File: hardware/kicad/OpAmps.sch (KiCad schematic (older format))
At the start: 63 parts, among them P1 Out X, P2 Out Y, P3 Out Red, P4 Out Green, P5 Out Blue, P6 Out C1, U2 LT1356CN, U3 LT1356CN, U4 LT1356CN

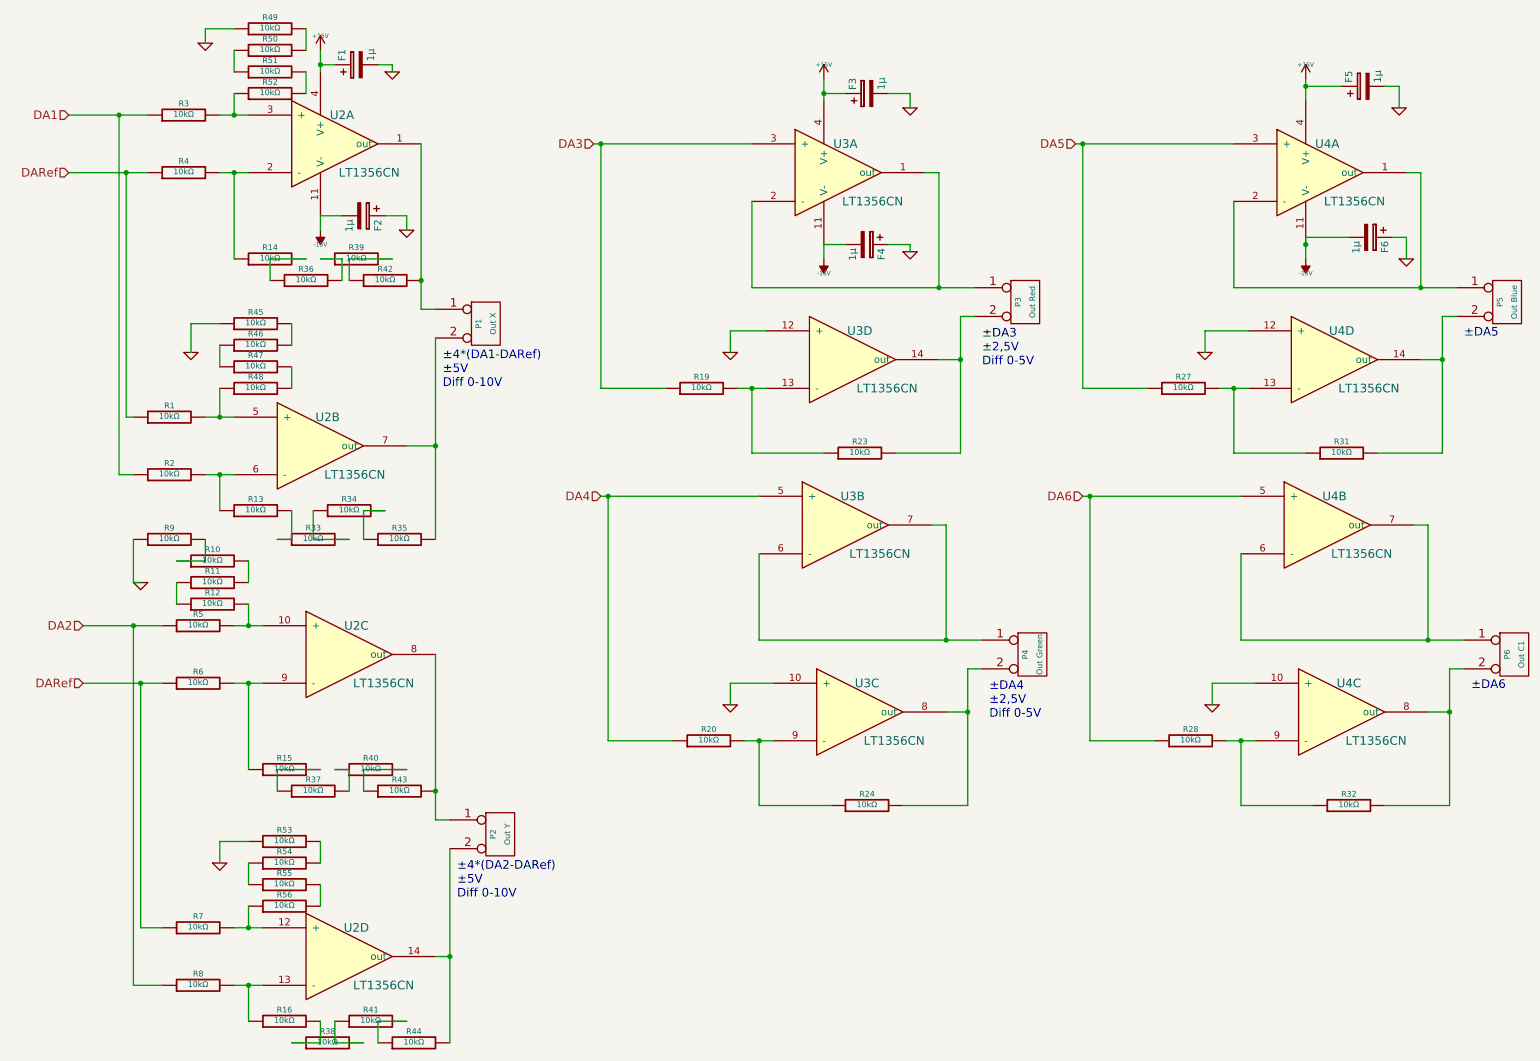
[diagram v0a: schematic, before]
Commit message: add output protection
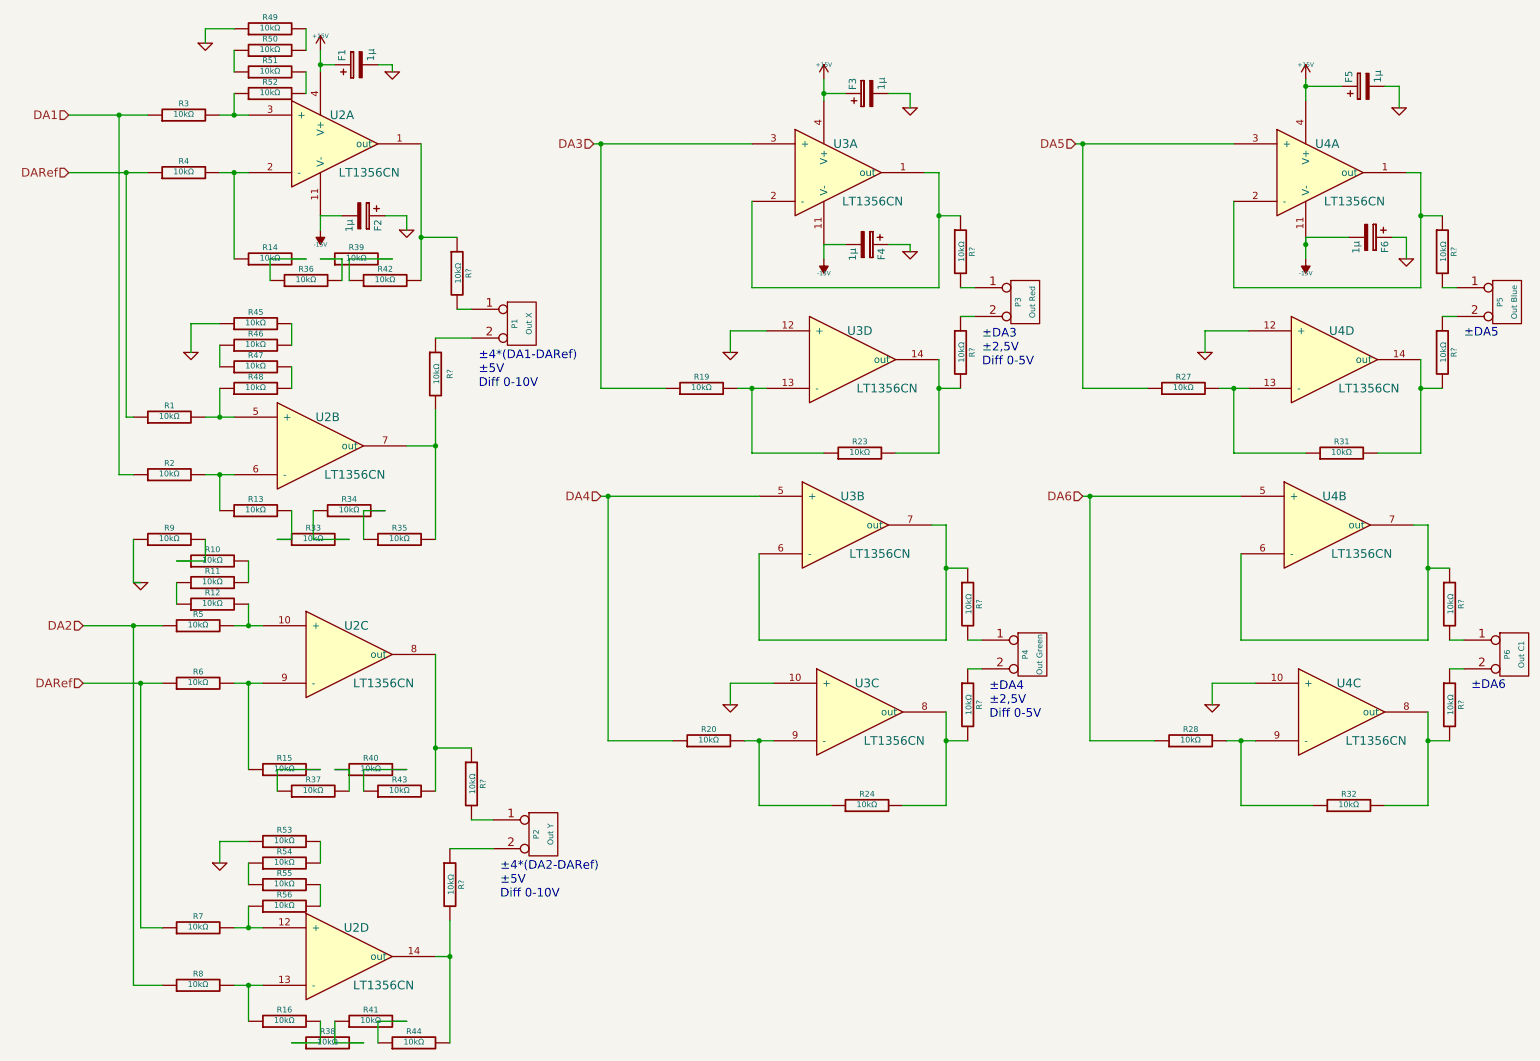
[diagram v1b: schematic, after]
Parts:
- added R? (x4): 10kΩ, Resistors_SMD:R_0603_HandSoldering, symbol R-RESCUE-ildagenerator
- added R? (x8): 10kΩ, symbol R-RESCUE-ildagenerator
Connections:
- net at R43.2, U2.8 (out): now also R?.1; no longer P2.1 (P1)
- net at R35.2, U2.7 (out): now also R?.2; no longer P1.2 (PM)
- net at R44.2, U2.14 (out): now also R?.2; no longer P2.2 (PM)
- net at R42.2, U2.1 (out): now also R?.1; no longer P1.1 (P1)
- net at U3.1 (out), U3.2 (-): now also R?.1; no longer P3.1 (P1)
- net at R24.2, U3.8 (out): now also R?.2; no longer P4.2 (PM)
- net at R23.2, U3.14 (out): now also R?.2; no longer P3.2 (PM)
- net at U3.6 (-), U3.7 (out): now also R?.1; no longer P4.1 (P1)
- net at U4.1 (out), U4.2 (-): now also R?.1; no longer P5.1 (P1)
- net at R32.2, U4.8 (out): now also R?.2; no longer P6.2 (PM)
- net at R31.2, U4.14 (out): now also R?.2; no longer P5.2 (PM)
- net at U4.6 (-), U4.7 (out): now also R?.1; no longer P6.1 (P1)
- new net: P1.1 (P1), R?.2
- new net: P1.2 (PM), R?.1
- new net: P2.1 (P1), R?.2
- new net: P2.2 (PM), R?.1
- new net: P3.1 (P1), R?.2
- new net: P3.2 (PM), R?.1
- new net: P4.1 (P1), R?.2
- new net: P4.2 (PM), R?.1
- new net: P5.1 (P1), R?.2
- new net: P5.2 (PM), R?.1
- new net: P6.1 (P1), R?.2
- new net: P6.2 (PM), R?.1
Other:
- moved on the sheet: P1, P2

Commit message: rout output protection
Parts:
- gave numbers to parts that had none: 12
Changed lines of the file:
@@
 	2550 1000 2550 850
 $Comp
-L -15V #PWR6
+L -15V #PWR15
 U 1 1 53E1F14E
 P 2550 2100
-F 0 "#PWR6" H 2550 2230 20  0001 C CNN
+F 0 "#PWR15" H 2550 2230 20  0001 C CNN
 F 1 "-15V" H 2550 2200 30  0000 C CNN
 F 2 "" H 2550 2100 60  0001 C CNN
@@
 	6050 1050 6050 1200
 $Comp
-L -15V #PWR12
+L -15V #PWR21
 U 1 1 53E1F32F
 P 6050 2300
-F 0 "#PWR12" H 6050 2430 20  0001 C CNN
+F 0 "#PWR21" H 6050 2430 20  0001 C CNN
 F 1 "-15V" H 6050 2400 30  0000 C CNN
 F 2 "" H 6050 2300 60  0001 C CNN
@@
 $EndComp
 $Comp
-L -15V #PWR18
+L -15V #PWR27
 U 1 1 53E1F3D5
 P 9400 2300
-F 0 "#PWR18" H 9400 2430 20  0001 C CNN
+F 0 "#PWR27" H 9400 2430 20  0001 C CNN
 F 1 "-15V" H 9400 2400 30  0000 C CNN
 F 2 "" H 9400 2300 60  0001 C CNN
@@
 	8750 5250 9050 5250
 $Comp
-L R-RESCUE-ildagenerator R?
+L R-RESCUE-ildagenerator R21
 U 1 1 55DEDC4E
 P 3500 2400
-F 0 "R?" V 3580 2400 40  0000 C CNN
+F 0 "R21" V 3580 2400 40  0000 C CNN
 F 1 "10kΩ" V 3507 2401 40  0000 C CNN
 F 2 "Resistors_SMD:R_0603_HandSoldering" H 3500 2400 60  0001 C CNN
@@
 $EndComp
 $Comp
-L R-RESCUE-ildagenerator R?
+L R-RESCUE-ildagenerator R17
 U 1 1 55DEDD53
 P 3350 3100
-F 0 "R?" V 3450 3100 40  0000 C CNN
+F 0 "R17" V 3450 3100 40  0000 C CNN
 F 1 "10kΩ" V 3357 3101 40  0000 C CNN
 F 2 "Resistors_SMD:R_0603_HandSoldering" H 3350 3100 60  0001 C CNN
@@
 	3500 2650 3600 2650
 $Comp
-L R-RESCUE-ildagenerator R?
+L R-RESCUE-ildagenerator R22
 U 1 1 55E02ADD
 P 3600 5950
-F 0 "R?" V 3680 5950 40  0000 C CNN
+F 0 "R22" V 3680 5950 40  0000 C CNN
 F 1 "10kΩ" V 3607 5951 40  0000 C CNN
 F 2 "Resistors_SMD:R_0603_HandSoldering" H 3600 5950 60  0001 C CNN
@@
 $EndComp
 $Comp
-L R-RESCUE-ildagenerator R?
+L R-RESCUE-ildagenerator R18
 U 1 1 55E02BFC
 P 3450 6650
-F 0 "R?" V 3530 6650 40  0000 C CNN
+F 0 "R18" V 3530 6650 40  0000 C CNN
 F 1 "10kΩ" V 3457 6651 40  0000 C CNN
 F 2 "Resistors_SMD:R_0603_HandSoldering" H 3450 6650 60  0001 C CNN
@@
 	3750 6200 3600 6200
 $Comp
-L R-RESCUE-ildagenerator R?
+L R-RESCUE-ildagenerator R29
 U 1 1 55E130AE
 P 7050 4700
-F 0 "R?" V 7130 4700 40  0000 C CNN
+F 0 "R29" V 7130 4700 40  0000 C CNN
 F 1 "10kΩ" V 7057 4701 40  0000 C CNN
 F 2 "" H 7050 4700 60  0001 C CNN
@@
 $EndComp
 $Comp
-L R-RESCUE-ildagenerator R?
+L R-RESCUE-ildagenerator R30
 U 1 1 55E13217
 P 7050 5400
-F 0 "R?" V 7130 5400 40  0000 C CNN
+F 0 "R30" V 7130 5400 40  0000 C CNN
 F 1 "10kΩ" V 7057 5401 40  0000 C CNN
 F 2 "" H 7050 5400 60  0001 C CNN
@@
 	7150 5150 7050 5150
 $Comp
-L R-RESCUE-ildagenerator R?
+L R-RESCUE-ildagenerator R26
 U 1 1 55E210D5
 P 7000 2950
-F 0 "R?" V 7080 2950 40  0000 C CNN
+F 0 "R26" V 7080 2950 40  0000 C CNN
 F 1 "10kΩ" V 7007 2951 40  0000 C CNN
 F 2 "" H 7000 2950 60  0001 C CNN
@@
 	6850 2500 5550 2500
 $Comp
-L R-RESCUE-ildagenerator R?
+L R-RESCUE-ildagenerator R25
 U 1 1 55E22292
 P 7000 2250
-F 0 "R?" V 7080 2250 40  0000 C CNN
+F 0 "R25" V 7080 2250 40  0000 C CNN
 F 1 "10kΩ" V 7007 2251 40  0000 C CNN
 F 2 "" H 7000 2250 60  0001 C CNN
@@
 	7100 2500 7000 2500
 $Comp
-L R-RESCUE-ildagenerator R?
+L R-RESCUE-ildagenerator R57
 U 1 1 55E24449
 P 10350 2250
-F 0 "R?" V 10430 2250 40  0000 C CNN
+F 0 "R57" V 10430 2250 40  0000 C CNN
 F 1 "10kΩ" V 10357 2251 40  0000 C CNN
 F 2 "" H 10350 2250 60  0001 C CNN
@@
 	10350 2500 10450 2500
 $Comp
-L R-RESCUE-ildagenerator R?
+L R-RESCUE-ildagenerator R58
 U 1 1 55E25906
 P 10350 2950
-F 0 "R?" V 10430 2950 40  0000 C CNN
+F 0 "R58" V 10430 2950 40  0000 C CNN
 F 1 "10kΩ" V 10357 2951 40  0000 C CNN
 F 2 "" H 10350 2950 60  0001 C CNN
@@
 	10250 6100 9950 6100
 $Comp
-L R-RESCUE-ildagenerator R?
+L R-RESCUE-ildagenerator R60
 U 1 1 55E2D9FA
 P 10400 5400
-F 0 "R?" V 10480 5400 40  0000 C CNN
+F 0 "R60" V 10480 5400 40  0000 C CNN
 F 1 "10kΩ" V 10407 5401 40  0000 C CNN
 F 2 "" H 10400 5400 60  0001 C CNN
@@
 	10400 5150 10500 5150
 $Comp
-L R-RESCUE-ildagenerator R?
+L R-RESCUE-ildagenerator R59
 U 1 1 55E2ED6B
 P 10400 4700
-F 0 "R?" V 10480 4700 40  0000 C CNN
+F 0 "R59" V 10480 4700 40  0000 C CNN
 F 1 "10kΩ" V 10407 4701 40  0000 C CNN
 F 2 "" H 10400 4700 60  0001 C CNN

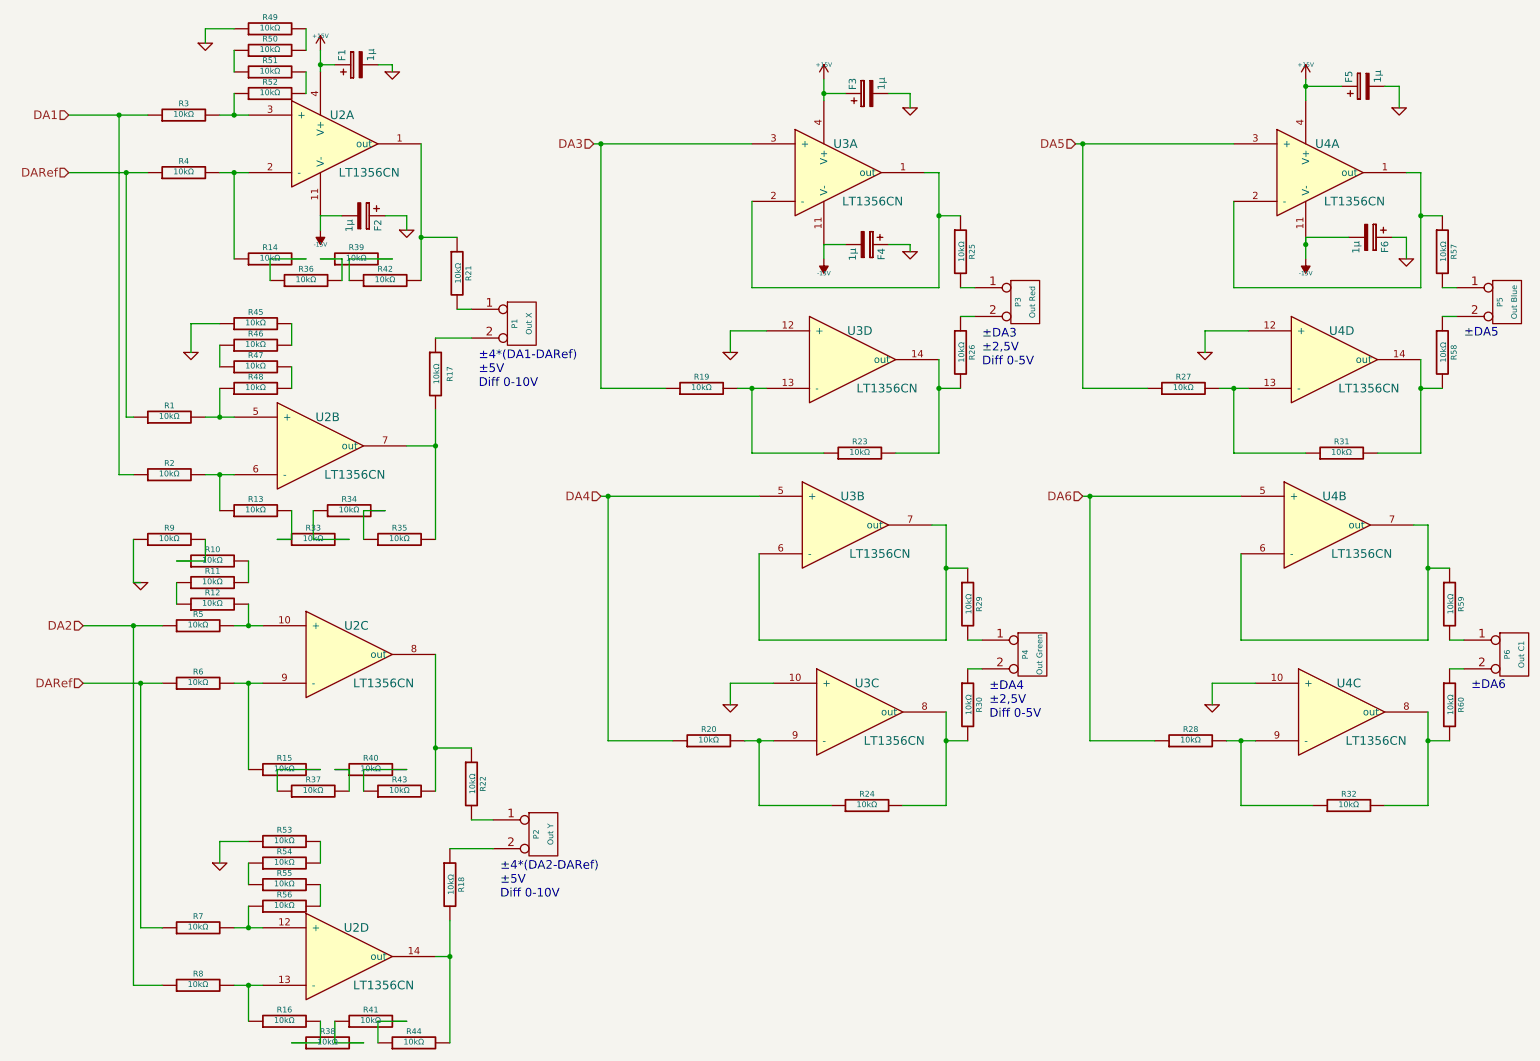
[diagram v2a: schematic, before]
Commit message: mov output protect
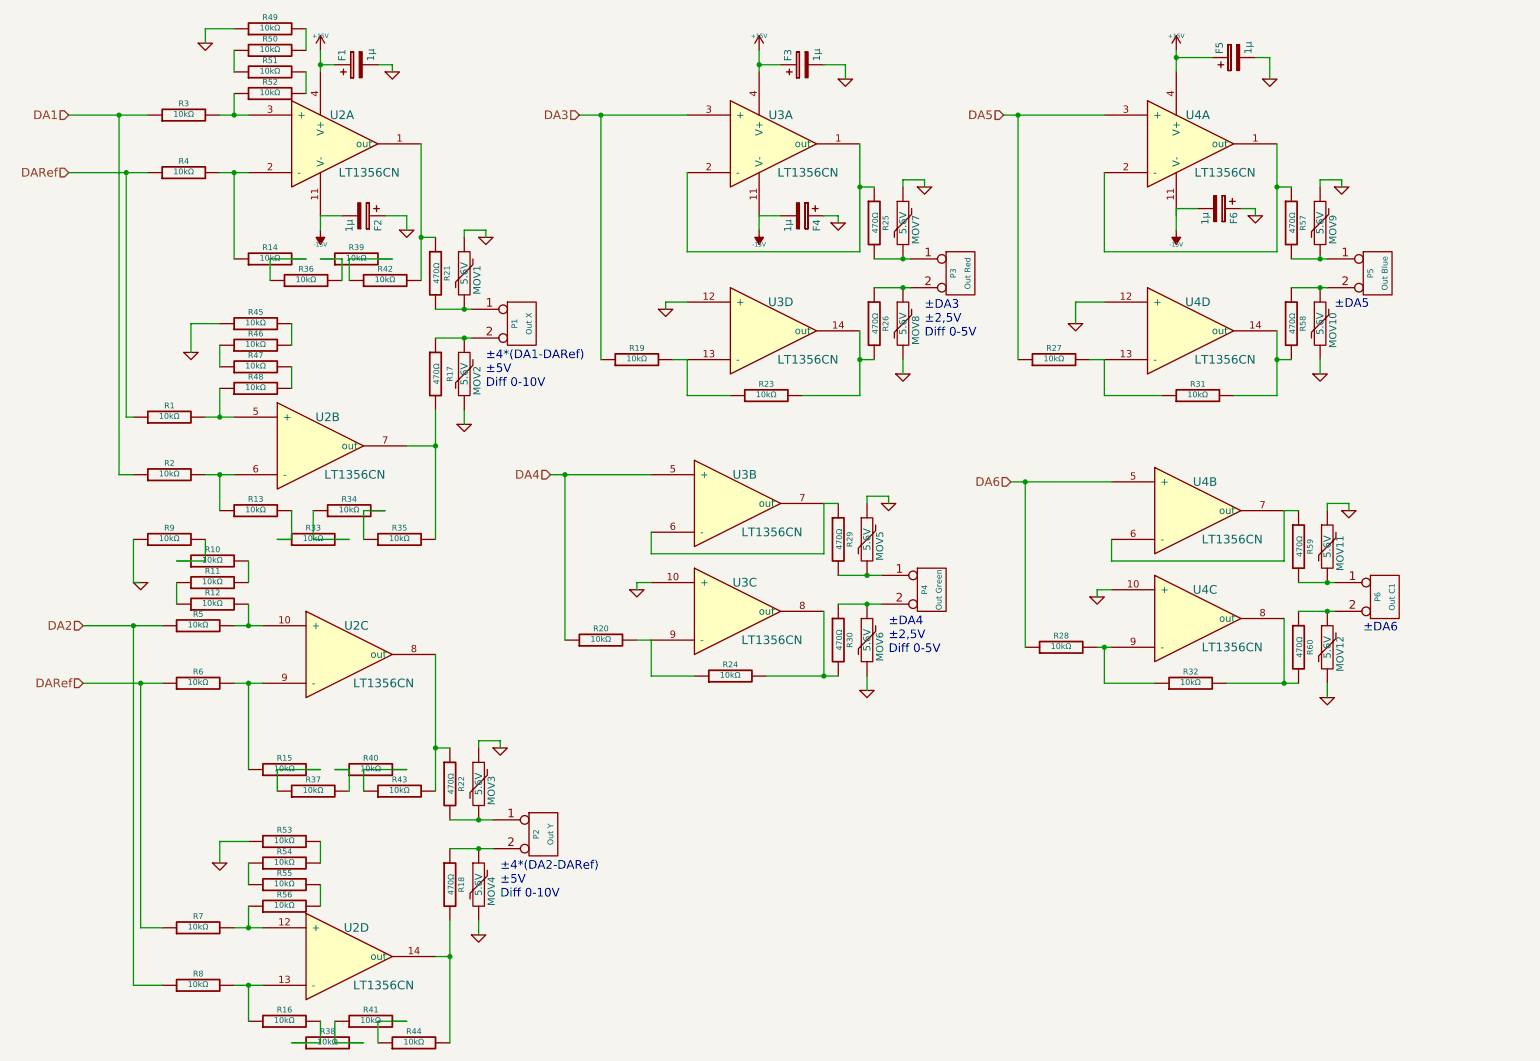
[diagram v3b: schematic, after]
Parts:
- added MOV1, MOV10, MOV11, MOV12, MOV2, MOV3, MOV4, MOV5, MOV6, MOV7, MOV8, MOV9: 5.6V, Resistors_SMD:R_1206_HandSoldering, symbol VR
- R17, R18, R21, R22, R25, R26, R29, R30, R57, R58, R59, R60: value 10kΩ -> 470Ω
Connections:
- net -15V: no longer U4.11 (V-)
- net GND: now also MOV1.1, MOV10.2, MOV11.1, MOV12.2, MOV2.2, MOV3.1, MOV4.2, MOV5.1, MOV6.2, MOV7.1, MOV8.2, MOV9.1
- net at P1.1 (P1), R21.2: now also MOV1.2
- net at P1.2 (PM), R17.1: now also MOV2.1
- net at P2.1 (P1), R22.2: now also MOV3.2
- net at P2.2 (PM), R18.1: now also MOV4.1
- net at P3.1 (P1), R25.2: now also MOV7.2
- net at P3.2 (PM), R26.1: now also MOV8.1
- net at P4.1 (P1), R29.2: now also MOV5.2
- net at P4.2 (PM), R30.1: now also MOV6.1
- net at P5.1 (P1), R57.2: now also MOV9.2
- net at P5.2 (PM), R58.1: now also MOV10.1
- net at P6.1 (P1), R59.2: now also MOV11.2
- net at P6.2 (PM), R60.1: now also MOV12.1
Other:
- moved on the sheet: F3, F4, F5, F6, P3, P4, P5, P6, R19, R20, R21, R22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

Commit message: placing movs
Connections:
- net -15V: now also U4.11 (V-)
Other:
- moved on the sheet: F6
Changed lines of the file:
@@
 	-1   0    0    1
 $EndComp
-Wire Wire Line
-	8500 1950 8500 2100
 $Comp
 L GND-RESCUE-ildagenerator #PWR32
@@
 L GND-RESCUE-ildagenerator #PWR36
 U 1 1 55C0D931
-P 9050 2000
-F 0 "#PWR36" H 9050 2000 30  0001 C CNN
-F 1 "GND" H 9050 1930 30  0001 C CNN
-F 2 "" H 9050 2000 60  0001 C CNN
-F 3 "" H 9050 2000 60  0001 C CNN
-	1    9050 2000
+P 9050 2050
+F 0 "#PWR36" H 9050 2050 30  0001 C CNN
+F 1 "GND" H 9050 1980 30  0001 C CNN
+F 2 "" H 9050 2050 60  0001 C CNN
+F 3 "" H 9050 2050 60  0001 C CNN
+	1    9050 2050
 	1    0    0    -1
 $EndComp
@@
 L CP F6
 U 1 1 55C0D720
-P 8800 1950
-F 0 "F6" H 8825 2050 50  0000 L CNN
-F 1 "1µ" H 8825 1850 50  0000 L CNN
-F 2 "Capacitors_Tantalum_SMD:TantalC_SizeB_EIA-3528_HandSoldering" H 8838 1800 30  0001 C CNN
-F 3 "" H 8800 1950 60  0000 C CNN
-	1    8800 1950
+P 8800 2000
+F 0 "F6" H 8825 2100 50  0000 L CNN
+F 1 "1µ" H 8825 1900 50  0000 L CNN
+F 2 "Capacitors_Tantalum_SMD:TantalC_SizeB_EIA-3528_HandSoldering" H 8838 1850 30  0001 C CNN
+F 3 "" H 8800 2000 60  0000 C CNN
+	1    8800 2000
 	0    1    1    0
 $EndComp
-Wire Wire Line
-	8650 1950 8500 1950
-Wire Wire Line
-	8950 1950 9050 1950
-Wire Wire Line
-	9050 1950 9050 2000
 Wire Wire Line
 	9200 1500 9200 2250
@@
 Wire Wire Line
 	7350 3850 8050 3850
+Wire Wire Line
+	8500 2000 8500 2100
+Wire Wire Line
+	8500 2000 8650 2000
+Wire Wire Line
+	8950 2000 9050 2000
+Wire Wire Line
+	9050 2000 9050 2050
 $EndSCHEMATC

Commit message: documentation
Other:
- note added: "±4*(DA1-DARef)\n±5V\nDiff -10V to +10V"
- note added: "±4*(DA2-DARef)\n±5V\nDiff -10V to +10V"
- note added: "±DA3\n±2,5V\nDiff 0V to +5V"
- note added: "±DA4\n±2,5V\nDiff 0V to +5V"
- note added: "±DA5\n±2,5V\nDiff 0V to +5V"
- note added: "±DA6\n±2,5V\nDiff 0V to +5V"
- note removed: "±4*(DA1-DARef)\n±5V\nDiff 0-10V"
- note removed: "±4*(DA2-DARef)\n±5V\nDiff 0-10V"
- note removed: "±DA3\n±2,5V\nDiff 0-5V"
- note removed: "±DA4\n±2,5V\nDiff 0-5V"
- note removed: "±DA5"
- note removed: "±DA6"
- moved on the sheet: F5, F6, MOV10, MOV9, P5, R27, R31, R57, R58, U4A, U4D
